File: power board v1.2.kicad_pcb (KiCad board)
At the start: 2 copper layers, 63.5 x 90.8 mm, 36 parts, among them J1 Conn_01x02_Female, J11 Conn_01x02_Female, J12 Conn_01x02_Female, J2 Conn_01x02_Female, J3 Conn_01x02_Female, J4 Conn_01x02_Female, J5 Conn_01x02_Female, J6 Conn_01x02_Female, J7 Conn_01x02_Female, J8 Conn_01x02_Female, J9 Conn_01x02_Female, Q1 STP160N3LL, U1 THL-25-2411

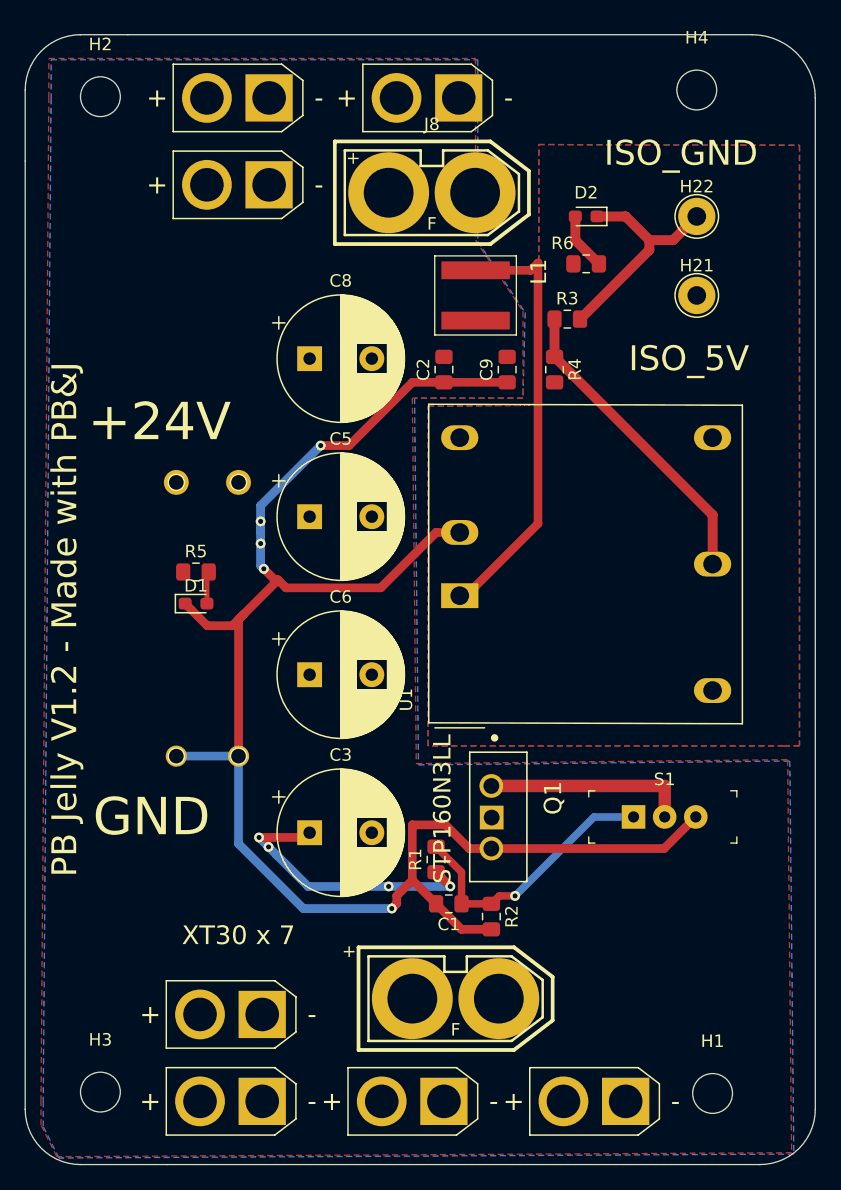
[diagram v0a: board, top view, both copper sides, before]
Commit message: added leds annd switch and decreased size
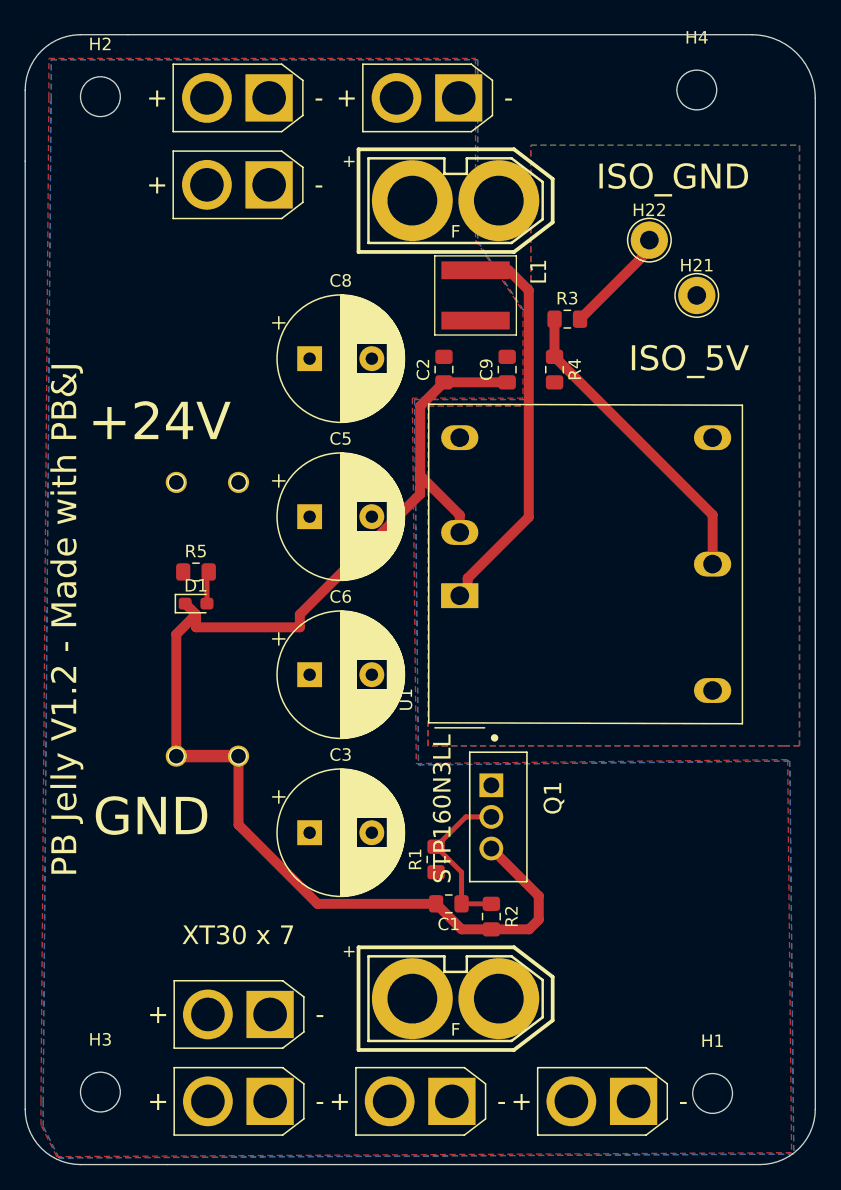
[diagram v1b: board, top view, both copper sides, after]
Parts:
- removed D2: LED, LED_SMD:LED_0603_1608Metric_Pad1.05x0.95mm_HandSolder
- removed J8: Conn_01x02_Female, RC-Battery-Connectors:XT-60_female
- removed R6: 10K, Resistor_SMD:R_0805_2012Metric_Pad1.15x1.40mm_HandSolder
- removed S1: EG1218, digikey-footprints:Switch_Slide_11.6x4mm_EG1218
- added J10: Conn_01x02_Female, RC-Battery-Connectors:XT-60_female, F.Cu at (55.5, 46.4)
- C1: value 3UF -> .1UF
- R1: value 500K -> 1K
- R2: value 1M -> 1K
- moved H22 4.26 mm to (71.1, 49.5)
- moved J2 0.63 mm to (40.6, 118.7)
- moved J5 0.63 mm to (55.2, 118.7)
- moved J6 0.63 mm to (40.6, 111.8)
- moved J3 0.63 mm to (69.8, 118.7)
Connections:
- Q1 pad 2: Net-(Q1-Pad2) -> Net-(C1-Pad1)
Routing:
- net GND: track 136.0 -> 103.8 mm, vias 5 -> 0
- net +24V: track 22.8 -> 0.00 mm, vias 4 -> 0
- net Net-(Q1-Pad2): track 16.4 -> 0.00 mm
- net ISO_GND_5V: track 18.3 -> 8.66 mm
- net Net-(C1-Pad1): track 22.2 -> 13.3 mm, vias 1 -> 0
- net Net-(D2-Pad2): track 4.60 -> 0.00 mm
- net Net-(L1-Pad2): track 34.9 -> 30.9 mm
